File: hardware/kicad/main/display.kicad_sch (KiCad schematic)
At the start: 26 parts, among them J20 OLED_ZIF30, Q20 AO3401A, Q21 2N7002, U20 TPS61040DBVR

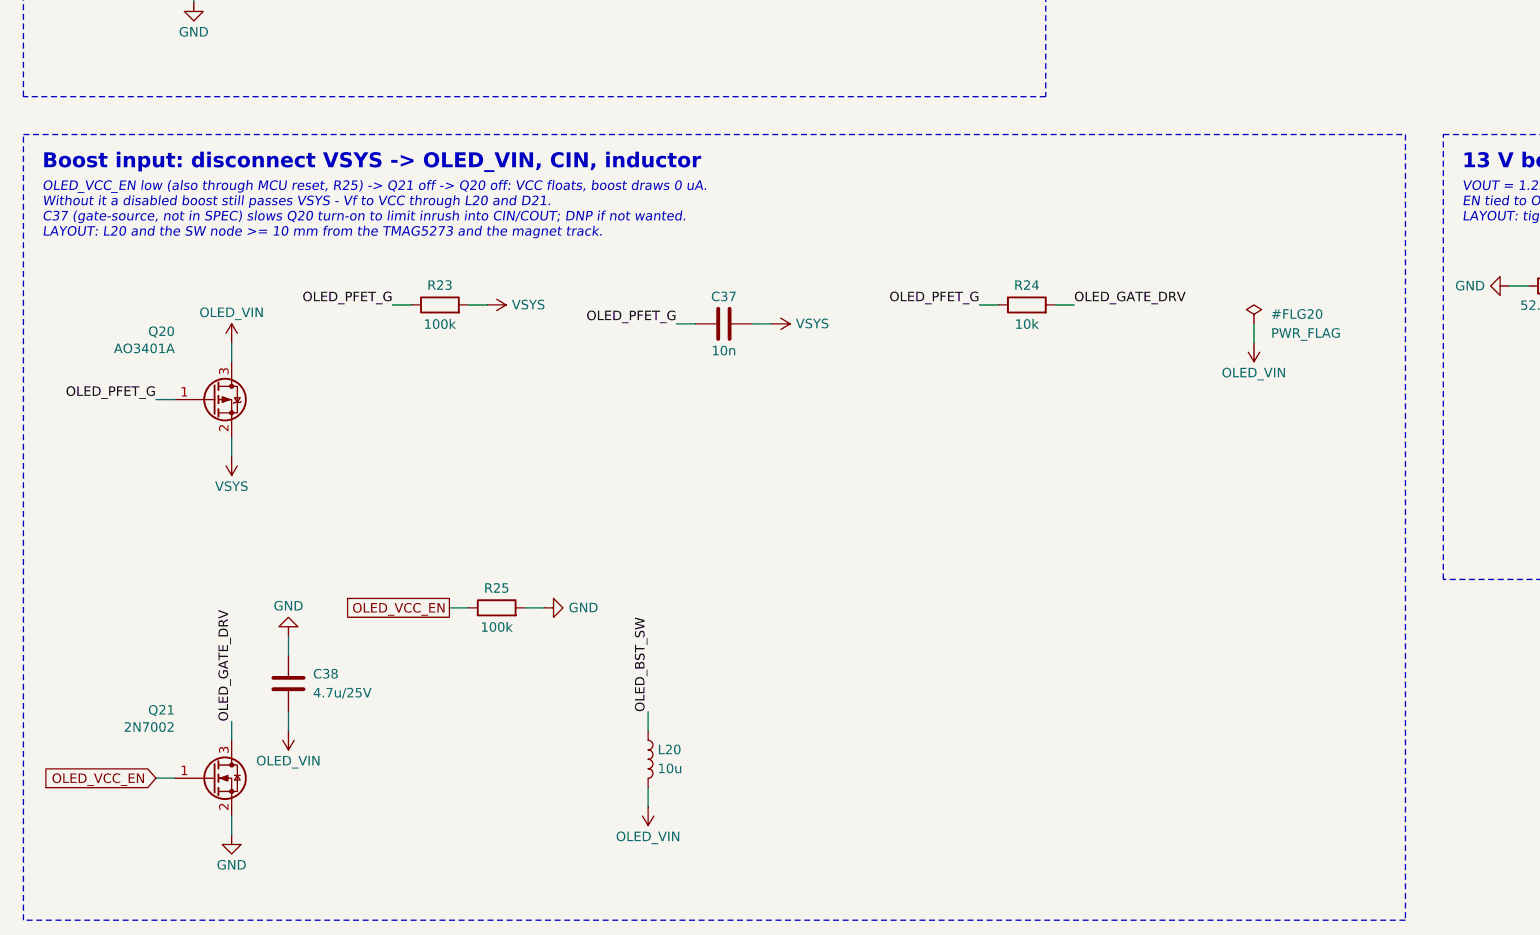
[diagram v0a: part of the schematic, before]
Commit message: Apply schematic review fixes; base board routes to 100% with zero DRC errors
- OLED VCC input disconnect is now a TPS22917 load switch (CT to VIN) instead
  of an AO3401A/2N7002 with no real inrush control
- TPD4E05U06 TVS on the TMAG5273 lines (floating 316L ring passes 2.4 mm away)
- piezo: 470R series + 1M bleed; LED_DIN pull-down moved to the shifter input
- base: explicit 2x4 DSBGA fan-out for the BQ25180, 0.4 mm power tracks,
  BAT+/GND silkscreen at the battery connector, JEITA NTC over the pack
- SPEC: side-entry link headers on both boards, 28 AWG power leads

Co-Authored-By: Claude Opus 5.5 <noreply@anthropic.com>
Claude-Session: https://claude.ai/code/session_01P3cqdBhxLcWY3sGUVf9LAJ
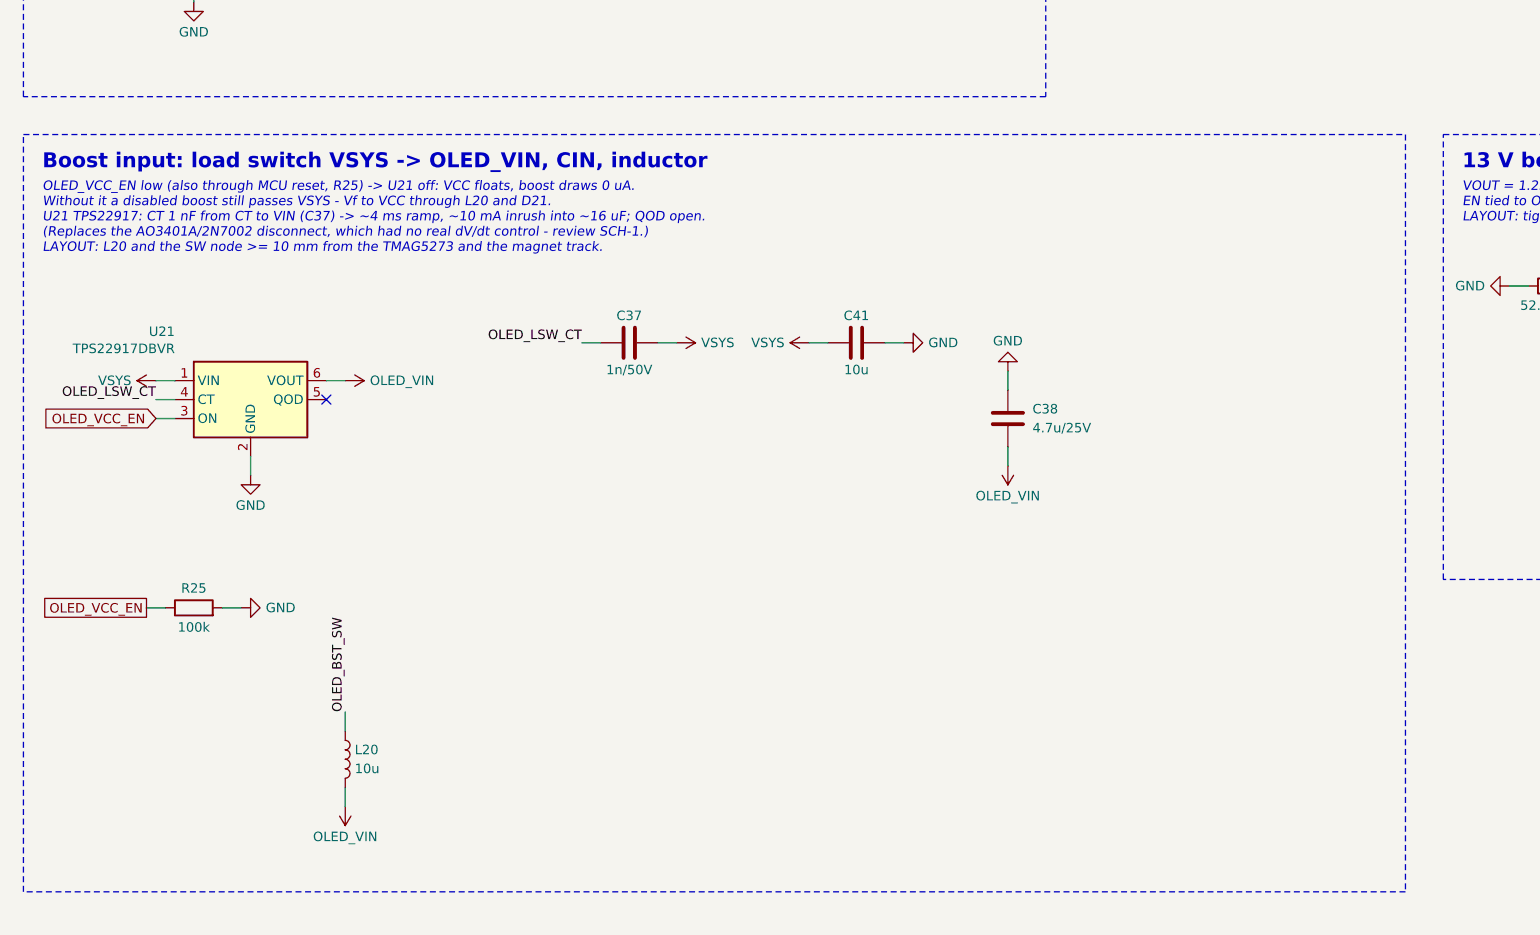
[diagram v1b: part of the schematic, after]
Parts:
- removed Q20: AO3401A, Package_TO_SOT_SMD:SOT-23, symbol Transistor_FET:AO3401A
- removed Q21: 2N7002, Package_TO_SOT_SMD:SOT-23, symbol Transistor_FET:2N7002
- removed R23: 100k, Resistor_SMD:R_0402_1005Metric, symbol Device:R
- removed R24: 10k, Resistor_SMD:R_0402_1005Metric, symbol Device:R
- added C41: 10u, Capacitor_SMD:C_0603_1608Metric, symbol Device:C
- added U21: TPS22917DBVR, Package_TO_SOT_SMD:SOT-23-6, symbol Power_Management:TPS22917DBV
- C37: value 10n -> 1n/50V; LCSC C15195 -> C1523; MPN CL05B103KB5NNNC -> 0402B102K500NT; Manufacturer Samsung Electro-Mechanics -> FH
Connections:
- net GND: now also C41.2, U21.2 (GND)
- net OLED_VCC_EN: now also U21.3 (ON)
- net OLED_VIN: now also U21.6 (VOUT)
- net VSYS: now also C41.1, U21.1 (VIN)
- net OLED_PFET_G renamed OLED_LSW_CT
- net OLED_LSW_CT: now also U21.4 (CT)
- no-connect marks 7 -> 8
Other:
- note added: "Boost input: load switch VSYS -> OLED_VIN, CIN, inductor"
- note added: "OLED_VCC_EN low (also through MCU reset, R25) -> U21 off: VCC floats, boost draws 0 uA. Without it a disabled boost still passes VSYS - Vf to VCC through L20 and D21. U21 TPS22917: CT 1 nF from CT to VIN (C37) -> ~4 ms ramp, ~10 mA inrush into ~16 uF; QOD open. (Replaces the AO3401A/2N7002 disconnect, which had no real dV/dt control - review SCH-1.) LAYOUT: L20 and the SW node >= 10 mm from the T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"
- note removed: "Boost input: disconnect VSYS -> OLED_VIN, CIN, inductor"
- note removed: "OLED_VCC_EN low (also through MCU reset, R25) -> Q21 off -> Q20 off: VCC floats, boost draws 0 uA. Without it a disabled boost still passes VSYS - Vf to VCC through L20 and D21. C37 (gate-source, not in SPEC) slows Q20 turn-on to limit inrush into CIN/COUT; DNP if not wanted. LAYOUT: L20 and the SW node >= 10 mm from the TMAG5273 and the magnet track."
- moved on the sheet: C37, C38, L20, R25

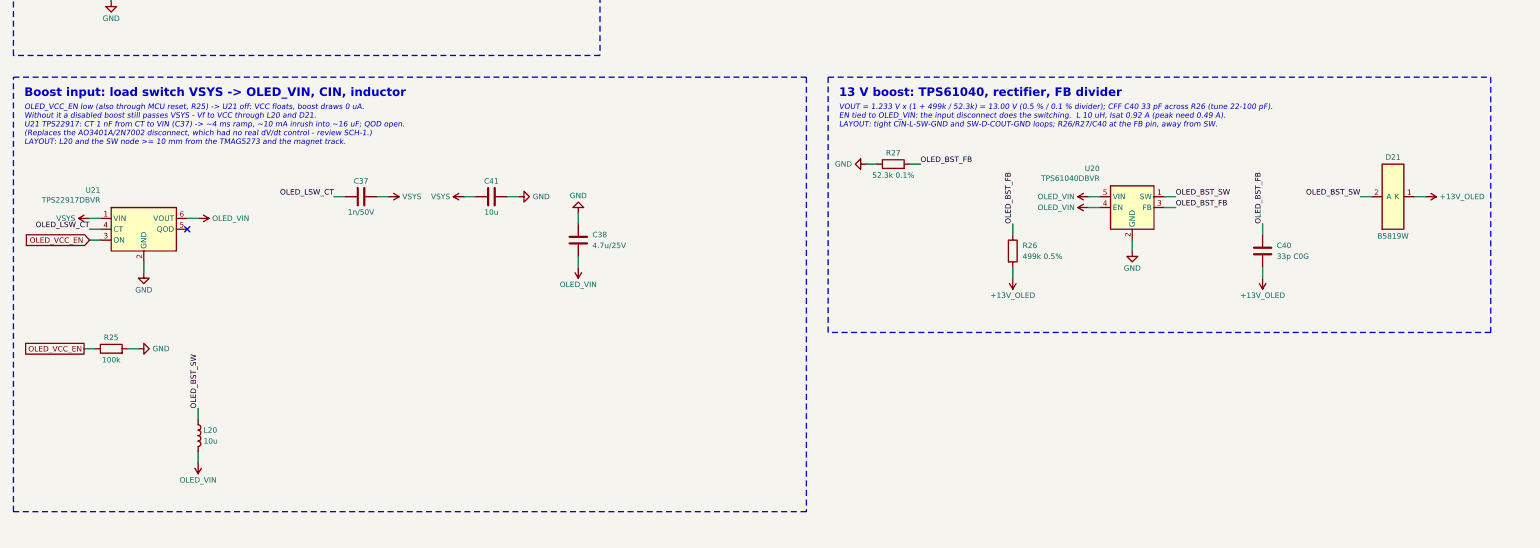
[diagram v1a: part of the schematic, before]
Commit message: Main schematic: ERC clean (VBUS_NRF power flag, documented waiver for U21 QOD tied to VOUT); Freerouting pass cap; load-switch test numerics fallback
- build.py: ERC_WAIVERS lists intended pin-type violations; waived ones are reported as such, never dropped
- mcu.py: PWR_FLAG on VBUS_NRF (fed from VBUS through R12)
- display.py: L20 note gives Isat 0.72 A rated (0.92 A typical)
- layout.py: also pass --router.max_passes (Freerouting 2.1 ignores -mp)
- test_load_switches.py: run() retries stalled/hung decks with looser numerics (verifier NEW-6)

Co-Authored-By: Claude Opus 5.5 <noreply@anthropic.com>
Claude-Session: https://claude.ai/code/session_01P3cqdBhxLcWY3sGUVf9LAJ
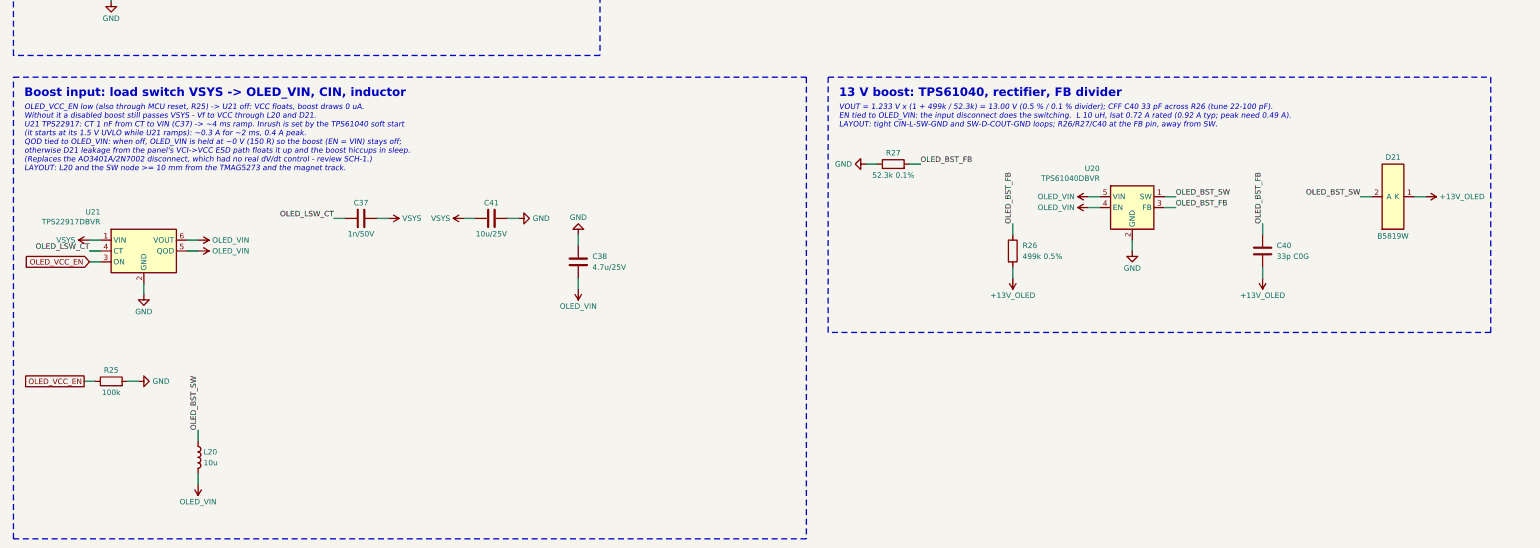
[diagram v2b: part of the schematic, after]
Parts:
- C41: value 10u -> 10u/25V; LCSC C19702 -> C96446; MPN CL10A106KP8NNNC -> CL10A106MA8NRNC
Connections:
- net OLED_VIN: now also U21.5 (QOD)
- no-connect marks 8 -> 7
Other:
- note added: "OLED_VCC_EN low (also through MCU reset, R25) -> U21 off: VCC floats, boost draws 0 uA. Without it a disabled boost still passes VSYS - Vf to VCC through L20 and D21. U21 TPS22917: CT 1 nF from CT to VIN (C37) -> ~4 ms ramp. Inrush is set by the TPS61040 soft start (it starts at its 1.5 V UVLO while U21 ramps): ~0.3 A for ~2 ms, 0.4 A peak. QOD tied to OLED_VIN: when off, OLED_VIN is held at ~0 V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"
- note added: "VOUT = 1.233 V x (1 + 499k / 52.3k) = 13.00 V (0.5 % / 0.1 % divider); CFF C40 33 pF across R26 (tune 22-100 pF). EN tied to OLED_VIN: the input disconnect does the switching. L 10 uH, Isat 0.72 A rated (0.92 A typ; peak need 0.49 A). LAYOUT: tight CIN-L-SW-GND and SW-D-COUT-GND loops; R26/R27/C40 at the FB pin, away from SW."
- note removed: "OLED_VCC_EN low (also through MCU reset, R25) -> U21 off: VCC floats, boost draws 0 uA. Without it a disabled boost still passes VSYS - Vf to VCC through L20 and D21. U21 TPS22917: CT 1 nF from CT to VIN (C37) -> ~4 ms ramp, ~10 mA inrush into ~16 uF; QOD open. (Replaces the AO3401A/2N7002 disconnect, which had no real dV/dt control - review SCH-1.) LAYOUT: L20 and the SW node >= 10 mm from the T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"
- note removed: "VOUT = 1.233 V x (1 + 499k / 52.3k) = 13.00 V (0.5 % / 0.1 % divider); CFF C40 33 pF across R26 (tune 22-100 pF). EN tied to OLED_VIN: the input disconnect does the switching. L 10 uH, Isat 0.92 A (peak need 0.49 A). LAYOUT: tight CIN-L-SW-GND and SW-D-COUT-GND loops; R26/R27/C40 at the FB pin, away from SW."
- moved on the sheet: C37, C38, C41, L20, R25, U21
